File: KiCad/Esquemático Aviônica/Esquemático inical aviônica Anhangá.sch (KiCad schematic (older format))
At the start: 20 parts, among them J1 Conn_01x06_Female, J2 Conn_01x06_Female, J3 Conn_01x12_Female, J4 Conn_01x12_Female, J5 Screw_Terminal_01x02, J6 Conn_01x06_Male, J7 Screw_Terminal_01x02, J8 Conn_01x07_Female, Q1 IRF7403, U1 ME620933

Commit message: Revisão pós montagem
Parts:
- J5, J7: footprint TerminalBlock_4Ucon:TerminalBlock_4Ucon_1x02_P3.50mm_Horizontal -> TerminalBlock:TerminalBlock_bornier-2_P5.08mm
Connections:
- net VCC is gone; now on net +3V3: C1.1, J6.1 (Pin_1), J8.6 (Pin_6), U1.3 (VOUT)
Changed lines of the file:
@@
 F 0 "J5" H 3980 5042 50  0001 L CNN
 F 1 "Screw_Terminal_01x02" H 3980 4951 50  0001 L CNN
-F 2 "TerminalBlock_4Ucon:TerminalBlock_4Ucon_1x02_P3.50mm_Horizontal" H 3900 5050 50  0001 C CNN
+F 2 "TerminalBlock:TerminalBlock_bornier-2_P5.08mm" H 3900 5050 50  0001 C CNN
 F 3 "~" H 3900 5050 50  0001 C CNN
 	1    3900 5050
@@
 F 0 "J7" H 5380 2692 50  0001 L CNN
 F 1 "Screw_Terminal_01x02" H 5380 2601 50  0001 L CNN
-F 2 "TerminalBlock_4Ucon:TerminalBlock_4Ucon_1x02_P3.50mm_Horizontal" H 5300 2700 50  0001 C CNN
+F 2 "TerminalBlock:TerminalBlock_bornier-2_P5.08mm" H 5300 2700 50  0001 C CNN
 F 3 "~" H 5300 2700 50  0001 C CNN
 	1    5300 2700
@@
 Text GLabel 2300 4350 0    50   Input ~ 0
 D_OUTPUT_NÍQUEL
-Text GLabel 2300 4350 2    50   Input ~ 0
+Text GLabel 2550 4350 2    50   Input ~ 0
 D2
 Text GLabel 3350 3950 1    50   Input ~ 0
@@
 Text GLabel 4700 3350 0    50   Input ~ 0
 D8
+Wire Wire Line
+	2300 4350 2550 4350
+Text GLabel 6850 4250 1    50   Input ~ 0
++3V3
+Wire Wire Line
+	6850 4250 6850 4300
 $EndSCHEMATC

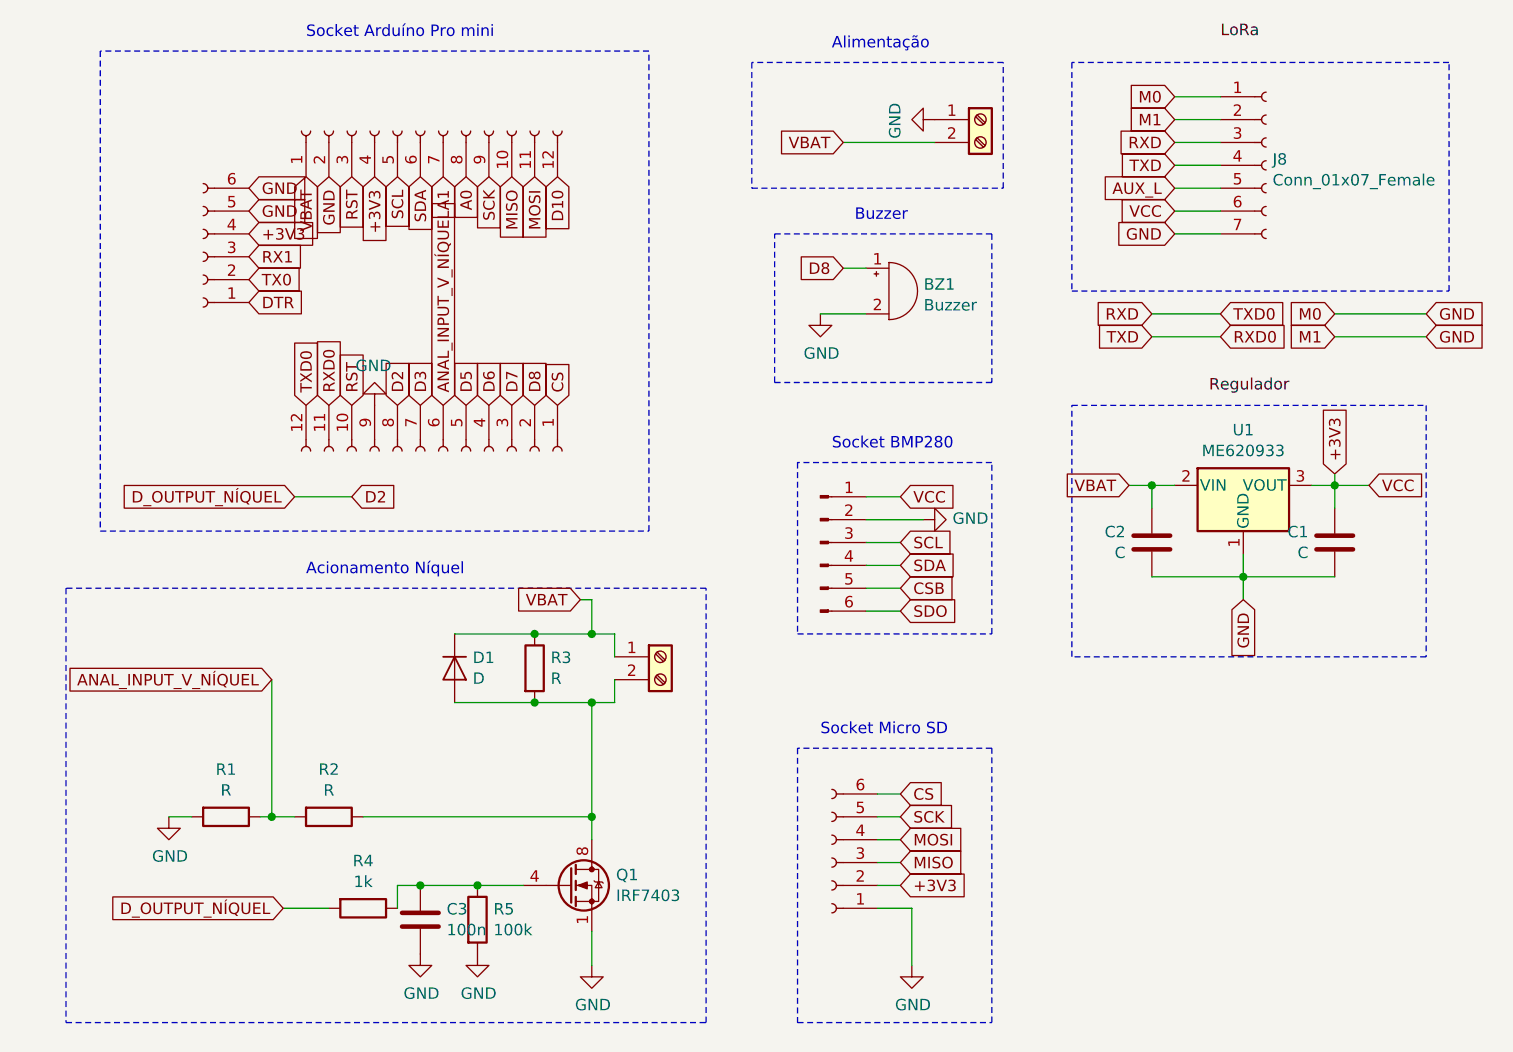
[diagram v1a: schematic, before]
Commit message: Adicionando novo BMP280
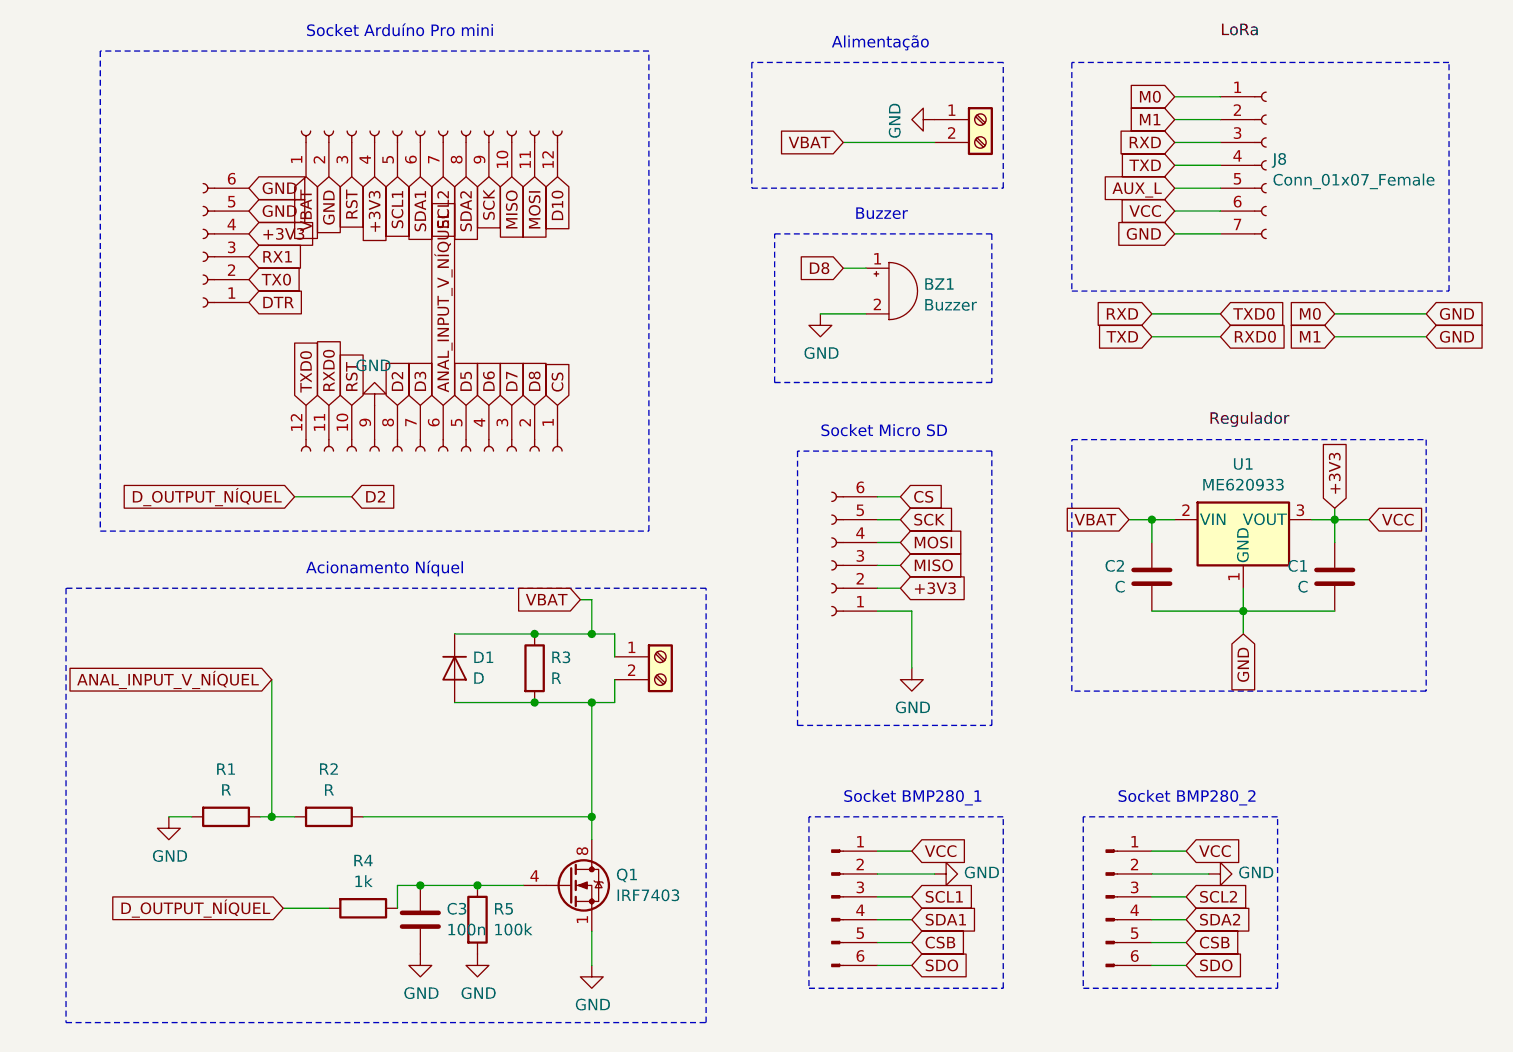
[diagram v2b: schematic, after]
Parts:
- added J9: Conn_01x06_Male, Connector_PinHeader_2.54mm:PinHeader_1x06_P2.54mm_Vertical, symbol Connector:Conn_01x06_Male
- C1, C2, C3: footprint Capacitor_SMD:C_0805_2012Metric_Pad1.15x1.40mm_HandSolder -> Capacitor_THT:C_Disc_D5.0mm_W2.5mm_P2.50mm
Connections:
- net +3V3: now also J9.1 (Pin_1)
- net CSB: now also J9.5 (Pin_5)
- net GND: now also J9.2 (Pin_2)
- net SDO: now also J9.6 (Pin_6)
- net A0 renamed SDA2
- net SDA2: now also J6.4 (Pin_4)
- net A1 renamed SCL2
- net SCL2: now also J6.3 (Pin_3)
- net SCL renamed SCL1
- net SCL1: now also J9.3 (Pin_3); no longer J6.3 (Pin_3)
- net SDA renamed SDA1
- net SDA1: now also J9.4 (Pin_4); no longer J6.4 (Pin_4)
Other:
- note added: "Socket BMP280_1\n"
- note added: "Socket BMP280_2\n"
- note removed: "Socket BMP280\n"
- moved on the sheet: C1, C2, U1

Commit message: Atualização Layout
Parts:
- removed J8: Conn_01x07_Female, Connector_PinSocket_2.54mm:PinSocket_1x07_P2.54mm_Vertical, symbol Connector:Conn_01x07_Female
- added J8: Conn_01x02_Female, Connector_PinSocket_2.54mm:PinSocket_1x02_P2.54mm_Vertical, symbol Connector:Conn_01x02_Female
- R1, R2, R3, R4, R5: footprint Resistor_SMD:R_0805_2012Metric_Pad1.15x1.40mm_HandSolder -> Resistor_THT:R_Axial_DIN0207_L6.3mm_D2.5mm_P5.08mm_Vertical
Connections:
- net CSB is gone; now on net VCC: J6.5 (Pin_5), J9.5 (Pin_5)
- net GND: now also J9.6 (Pin_6)
- net MISO: now also J3.11 (Pin_11); no longer J3.10 (Pin_10)
- net MOSI: now also J3.10 (Pin_10); no longer J3.11 (Pin_11)
- net +3V3 renamed VCC
- net VCC: now also J6.6 (Pin_6); no longer J2.4 (Pin_4), J3.4 (Pin_4)
- net RXD renamed D1
- net RXD0 renamed D0
- net SCL1 renamed A3
- net A3: no longer J9.3 (Pin_3)
- net SCL2 renamed A1
- net A1: no longer J6.3 (Pin_3)
- net SDA1 renamed A2
- net A2: no longer J9.4 (Pin_4)
- net SDA2 renamed A0
- net A0: no longer J6.4 (Pin_4)
- removed net SDO: J6.6 (Pin_6), J9.6 (Pin_6)
- new net 5V: J2.4 (Pin_4), J3.4 (Pin_4)
- new net SCL: J6.3 (Pin_3), J8.2 (Pin_2), J9.3 (Pin_3)
- new net SDA: J6.4 (Pin_4), J8.1 (Pin_1), J9.4 (Pin_4)
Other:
- moved on the sheet: BZ1, C1, C2, C3, D1, Q1, R1, R2, R3, R4, R5, U1

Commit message: Atualização Layout
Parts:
- J6, J9: footprint Connector_PinHeader_2.54mm:PinHeader_1x06_P2.54mm_Vertical -> Connector_PinSocket_2.54mm:PinSocket_1x06_P2.54mm_Vertical
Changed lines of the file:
@@
 F 0 "J6" H 5758 6389 50  0001 C CNN
 F 1 "Conn_01x06_Male" H 5758 6390 50  0001 C CNN
-F 2 "Connector_PinHeader_2.54mm:PinHeader_1x06_P2.54mm_Vertical" H 5650 6100 50  0001 C CNN
+F 2 "Connector_PinSocket_2.54mm:PinSocket_1x06_P2.54mm_Vertical" H 5650 6100 50  0001 C CNN
 F 3 "~" H 5650 6100 50  0001 C CNN
 	1    5650 6100
@@
 F 0 "J9" H 4758 6389 50  0001 C CNN
 F 1 "Conn_01x06_Male" H 4758 6390 50  0001 C CNN
-F 2 "Connector_PinHeader_2.54mm:PinHeader_1x06_P2.54mm_Vertical" H 4650 6100 50  0001 C CNN
+F 2 "Connector_PinSocket_2.54mm:PinSocket_1x06_P2.54mm_Vertical" H 4650 6100 50  0001 C CNN
 F 3 "~" H 4650 6100 50  0001 C CNN
 	1    4650 6100

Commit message: Atual. Layout + Esquemát.
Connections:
- net VBAT: now also J1.2 (Pin_2)
- net VCC: no longer J1.2 (Pin_2)
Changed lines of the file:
@@
 VBAT
 Text GLabel 5850 3200 2    50   Input ~ 0
-VCC
+VBAT
 Wire Notes Line
 	1450 2400 1450 4500
@@
 Wire Notes Line
 	6200 5400 4650 5400
-Text GLabel 5400 5150 3    50   Input ~ 0
-GND
 Text GLabel 4900 4650 0    50   Input ~ 0
 VBAT
@@
 Text GLabel 3250 2950 3    50   Input ~ 0
 MOSI
+$Comp
+L power:GND #PWR?
+U 1 1 5DB38D1B
+P 5400 5150
+F 0 "#PWR?" H 5400 4900 50  0001 C CNN
+F 1 "GND" H 5405 4977 50  0000 C CNN
+F 2 "" H 5400 5150 50  0001 C CNN
+F 3 "" H 5400 5150 50  0001 C CNN
+	1    5400 5150
+	1    0    0    -1
+$EndComp
 $EndSCHEMATC

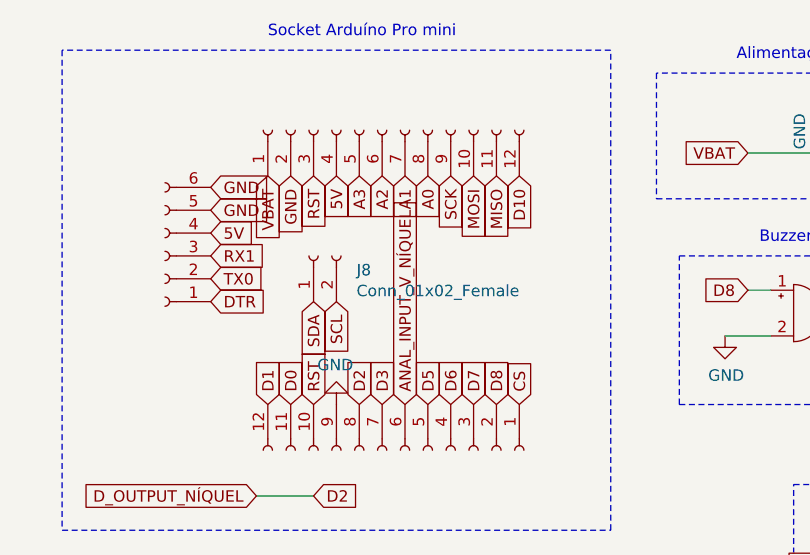
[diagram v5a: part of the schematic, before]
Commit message: Mudança de pinos
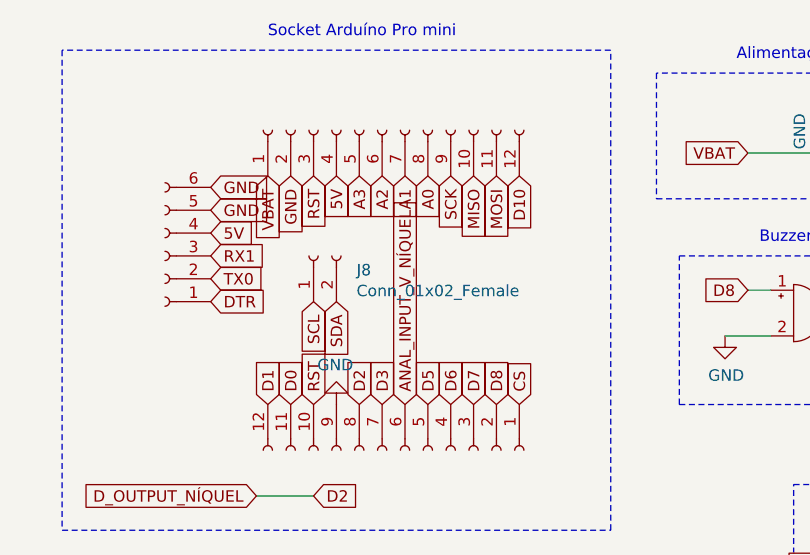
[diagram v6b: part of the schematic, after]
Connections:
- net MISO: now also J3.10 (Pin_10); no longer J3.11 (Pin_11)
- net MOSI: now also J3.11 (Pin_11); no longer J3.10 (Pin_10)
- net SCL: now also J8.1 (Pin_1); no longer J8.2 (Pin_2)
- net SDA: now also J8.2 (Pin_2); no longer J8.1 (Pin_1)
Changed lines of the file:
@@
 	0    -1   -1   0
 $EndComp
+Text GLabel 2650 3500 3    50   Input ~ 0
+SDA
 Text GLabel 2550 3500 3    50   Input ~ 0
-SDA
-Text GLabel 2650 3500 3    50   Input ~ 0
 SCL
 Text GLabel 3050 2950 3    50   Input ~ 0
@@
 	0    -1   -1   0
 $EndComp
+Text GLabel 3250 2950 3    50   Input ~ 0
+MISO
 Text GLabel 3350 2950 3    50   Input ~ 0
-MISO
-Text GLabel 3250 2950 3    50   Input ~ 0
 MOSI
 $Comp
-L power:GND #PWR?
+L power:GND #PWR0110
 U 1 1 5DB38D1B
 P 5400 5150
-F 0 "#PWR?" H 5400 4900 50  0001 C CNN
+F 0 "#PWR0110" H 5400 4900 50  0001 C CNN
 F 1 "GND" H 5405 4977 50  0000 C CNN
 F 2 "" H 5400 5150 50  0001 C CNN

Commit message: PCB Anhangá
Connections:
- net A0 is gone; now on net CS: J3.8 (Pin_8)
- net A1 is gone; now on net ANAL_INPUT_V_NÍQUEL: J3.7 (Pin_7)
- net 5V: now also J1.2 (Pin_2)
- net ANAL_INPUT_V_NÍQUEL: no longer J4.6 (Pin_6)
- net CS: no longer J4.1 (Pin_1)
- net D2: no longer R4.2
- net D8: now also R4.2; no longer BZ1.1 (-)
- net SCL: now also J8.2 (Pin_2); no longer J8.1 (Pin_1)
- net SDA: now also J8.1 (Pin_1); no longer J8.2 (Pin_2)
- net VBAT: no longer J1.2 (Pin_2)
- net D10 renamed 10
- net 10: now also BZ1.1 (-)
- new net D4: J4.6 (Pin_6)
- new net D9: J4.1 (Pin_1)
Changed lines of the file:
@@
 EESchema Schematic File Version 4
-LIBS:Esquemático inical aviônica Anhangá-cache
 EELAYER 30 0
 EELAYER END
@@
 Text GLabel 2100 3200 2    50   Input ~ 0
 5V
-Text GLabel 2950 2950 3    50   Input ~ 0
-A1
-Text GLabel 3450 3950 1    50   Input ~ 0
-CS
+Text GLabel 3450 2950 3    50   Input ~ 0
+10
 Text GLabel 3150 2950 3    50   Input ~ 0
 SCK
@@
 VBAT
 Text GLabel 5850 3200 2    50   Input ~ 0
-VBAT
+5V
 Wire Notes Line
 	1450 2400 1450 4500
@@
 Text GLabel 2550 3950 1    50   Input ~ 0
 RST
-Text GLabel 2950 3950 1    50   Input ~ 0
+Text GLabel 2950 2950 3    50   Input ~ 0
 ANAL_INPUT_V_NÍQUEL
 Text GLabel 3250 3950 1    50   Input ~ 0
@@
 Text GLabel 2550 2950 3    50   Input ~ 0
 RST
-Text GLabel 3450 2950 3    50   Input ~ 0
-D10
+Text GLabel 3450 3950 1    50   Input ~ 0
+D9
 Wire Notes Line
 	4650 4300 6200 4300
@@
 Text GLabel 2300 4350 0    50   Input ~ 0
 D_OUTPUT_NÍQUEL
-Text GLabel 2550 4350 2    50   Input ~ 0
-D2
 Text GLabel 3350 3950 1    50   Input ~ 0
 D8
 Text GLabel 4450 3450 0    50   Input ~ 0
-D8
+10
 Wire Wire Line
 	2300 4350 2550 4350
@@
 	0    -1   -1   0
 $EndComp
+Text GLabel 2550 3500 3    50   Input ~ 0
+SDA
 Text GLabel 2650 3500 3    50   Input ~ 0
-SDA
-Text GLabel 2550 3500 3    50   Input ~ 0
 SCL
-Text GLabel 3050 2950 3    50   Input ~ 0
-A0
 $Comp
 L Connector:Conn_01x02_Female J8
@@
 	1    0    0    -1
 $EndComp
+Text GLabel 2950 3950 1    50   Input ~ 0
+D4
+Text GLabel 3050 2950 3    50   Input ~ 0
+CS
+Text GLabel 2550 4350 2    50   Input ~ 0
+D8
 $EndSCHEMATC
